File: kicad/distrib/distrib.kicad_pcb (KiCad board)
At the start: 2 copper layers, 35 parts, among them J1 Conn_01x03_Male, J10 Conn_01x03_Male, J11 Conn_01x03_Male, J12 Conn_01x03_Male, J13 Conn_01x03_Male, J14 Conn_01x03_Male, J15 Conn_01x03_Male, J16 Conn_01x03_Male, J17 Conn_01x03_Male, J18 Conn_01x03_Male, J19 Conn_01x03_Male, J2 Conn_01x03_Male, J20 Conn_01x03_Male, J21 Conn_01x03_Male, J22 Conn_01x03_Male, J23 Conn_01x03_Male, J24 Conn_01x03_Male, J25 Conn_01x03_Male, J26 Conn_01x03_Male, J27 Conn_01x03_Male, J28 Conn_01x03_Male, J29 Conn_01x03_Male, J3 Conn_01x03_Male, J30 Conn_01x03_Male, J31 Screw_Terminal_01x02, J4 Conn_01x03_Male, J5 Conn_01x03_Male, J6 Conn_01x03_Male, J7 Conn_01x03_Male, J8 Conn_01x03_Male, J9 Conn_01x03_Male

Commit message: autosave
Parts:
- moved J31 72.4 mm to (40.6, 119.9)
- moved J11 69.9 mm to (40.6, 63.5)
- moved J12 69.9 mm to (50.8, 63.5)
- moved J14 69.9 mm to (40.6, 71.1)
- moved J15 69.9 mm to (50.8, 71.1)
- moved J2 69.9 mm to (40.6, 40.6)
- moved J20 69.9 mm to (40.6, 86.4)
- moved J21 69.9 mm to (50.8, 86.4)
- moved J23 69.9 mm to (40.6, 94.0)
- moved J24 69.9 mm to (50.8, 94.0)
- moved J26 69.9 mm to (40.6, 101.6)
- moved J27 69.9 mm to (50.8, 101.6)
- moved J29 69.9 mm to (40.6, 109.2)
- moved J3 69.9 mm to (50.8, 40.6)
- moved J30 69.9 mm to (50.8, 109.2)
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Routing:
- net +12V: track 251.4 -> 257.0 mm

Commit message: breakout
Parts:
- added J31: Conn_01x03_Male, Connectors_Phoenix:PhoenixContact_MCV-G_03x3.81mm_Vertical, F.Cu at (35.6, 33.0)
- added J32: Conn_01x03_Male, Connectors_Phoenix:PhoenixContact_MCV-G_03x3.81mm_Vertical, F.Cu at (53.3, 33.0)
- added J33: Conn_01x03_Male, Connectors_Phoenix:PhoenixContact_MCV-G_03x3.81mm_Vertical, F.Cu at (71.1, 33.0)
- added REF**: LOGO_RAT, zillo-mini-devkit:LOGO_RAT, B.Cu at (32.8, 179.8)
- J1, J10, J11, J12, J13, J14, J15, J16, J17, J18, J19, J2, J20, J21, J22, J23, J24, J25, J26, J27, J28, J29, J3, J30, J4, J5, J6, J7, J8, J9: footprint Connectors_Molex:Molex_KK-6410-03_03x2.54mm_Straight -> Connectors_Phoenix:PhoenixContact_MCV-G_03x3.81mm_Vertical
- POWER: renamed from J31; footprint Connectors_Molex:Molex_KK-6410-02_02x2.54mm_Straight -> Connector_AMASS:AMASS_XT60-F_1x02_P7.20mm_Vertical
- moved J3 121.1 mm to (71.1, 160.0)
- moved J2 120.1 mm to (53.3, 160.0)
- moved J1 119.5 mm to (35.6, 160.0)
- moved J6 101.1 mm to (71.1, 147.3)
- moved J5 99.9 mm to (53.3, 147.3)
- moved J4 99.2 mm to (35.6, 147.3)
- moved J9 81.3 mm to (71.1, 134.6)
- moved J8 79.8 mm to (53.3, 134.6)
- moved J7 78.9 mm to (35.6, 134.6)
- moved H3 77.4 mm to (86.4, 190.5)
- moved H4 71.2 mm to (27.9, 190.5)
- moved J30 66.7 mm to (71.1, 45.7)
- moved J29 64.8 mm to (53.3, 45.7)
- moved J28 63.7 mm to (35.6, 45.7)
- moved J12 61.9 mm to (71.1, 121.9)
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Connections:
- J30 pad 2: (no net) -> Net-(J30-Pad2)
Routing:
- net +12V: track 257.0 -> 484.3 mm
- net Net-(J30-Pad2): track 0.00 -> 41.9 mm
- net Net-(J32-Pad2): track 0.00 -> 21.2 mm
- net Net-(J18-Pad2): track 26.2 -> 43.0 mm
- net Net-(J12-Pad2): track 26.2 -> 41.9 mm
- net Net-(J6-Pad2): track 26.2 -> 41.9 mm
- net Net-(J24-Pad2): track 26.5 -> 41.9 mm
- net Net-(J2-Pad2): track 15.5 -> 21.2 mm
- net Net-(J26-Pad2): track 15.6 -> 21.2 mm
- net Net-(J28-Pad2): track 15.6 -> 21.2 mm
- net Net-(J4-Pad2): track 15.7 -> 21.2 mm
- net Net-(J20-Pad2): track 15.8 -> 21.2 mm
- net Net-(J10-Pad2): track 15.9 -> 21.2 mm
- net Net-(J14-Pad2): track 16.0 -> 21.2 mm
- net Net-(J16-Pad2): track 16.1 -> 21.2 mm
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- added copper zone on F.Cu, net GND
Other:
- board outline added: 68.6 x 175.3 mm
- board text added: "+"
- board text added: "-"
- board text added: "12V"
- board text added: "DrZoid 2020"
- board text added: "Zillominee Power Board V1.0"

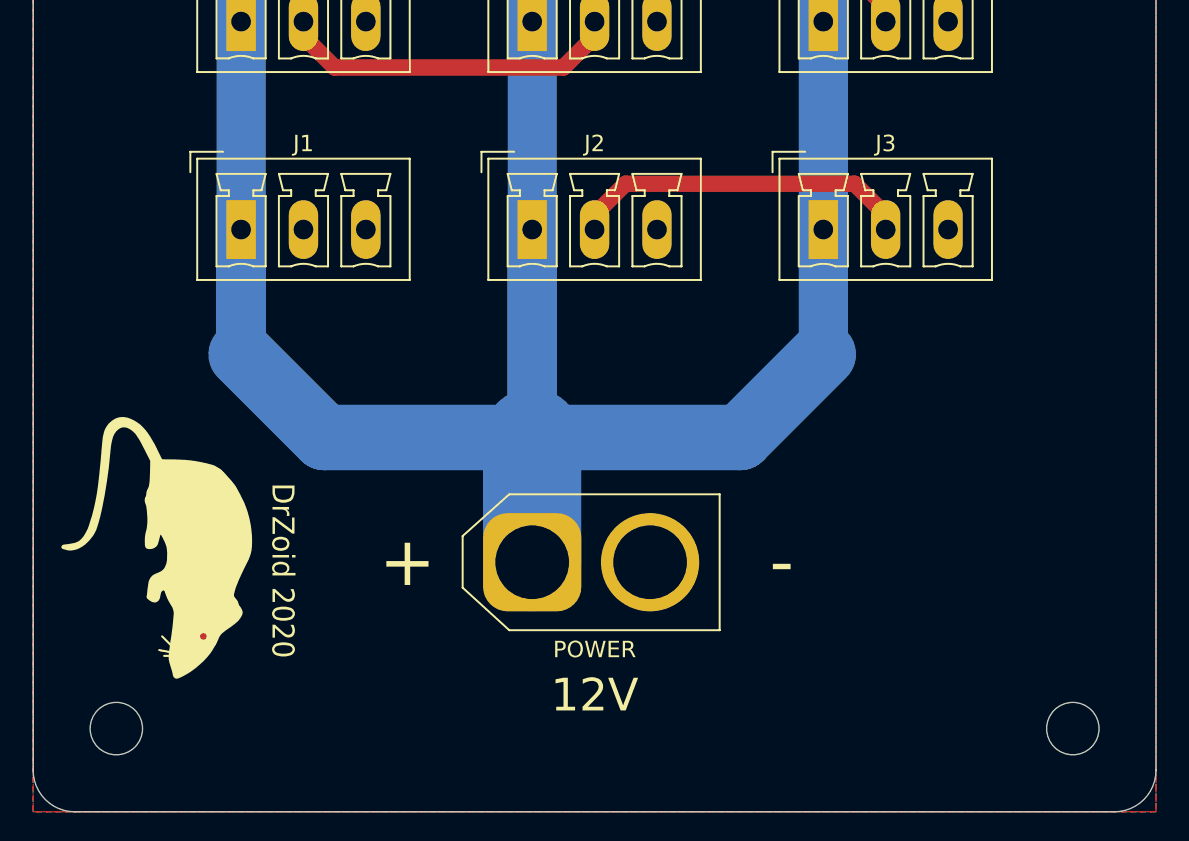
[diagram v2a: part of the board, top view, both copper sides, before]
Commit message: distrib: ajout connecteur leds
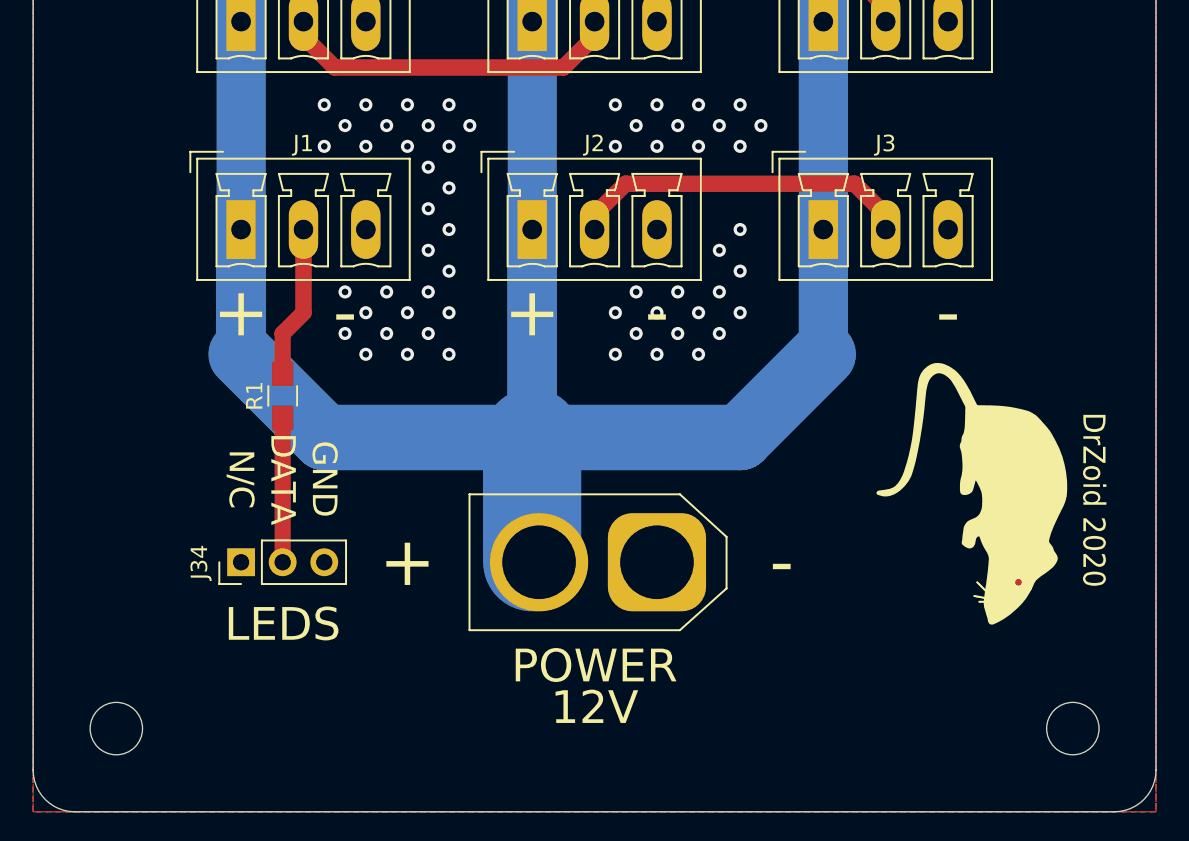
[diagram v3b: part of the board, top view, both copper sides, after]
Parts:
- added J34: LEDS, Pin_Headers:Pin_Header_Straight_1x03_Pitch2.54mm, F.Cu at (35.6, 180.3)
- added R1: 470, Resistors_SMD:R_0805_HandSoldering, F.Cu at (38.1, 170.2)
- POWER: value Screw_Terminal_01x02 -> XT60
- moved REF** 49.9 mm to (82.5, 176.5)
- moved POWER 7.62 mm to (61.0, 180.3), turned to 180 degrees
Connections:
- J1 pad 2: (no net) -> DATA_IN
- POWER pad 1: +12V -> GND
- POWER pad 2: GND -> +12V
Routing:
- net DATA_IN: track 0.00 -> 9.34 mm
- net Net-(J34-Pad2): track 0.00 -> 8.81 mm
- net GND: vias 0 -> 58
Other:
- board text added: "DATA"
- board text added: "GND"
- board text added: "N/C"
